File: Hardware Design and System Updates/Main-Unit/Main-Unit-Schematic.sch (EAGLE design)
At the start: 2 parts, among them U1 MSP430FR2110IPW16

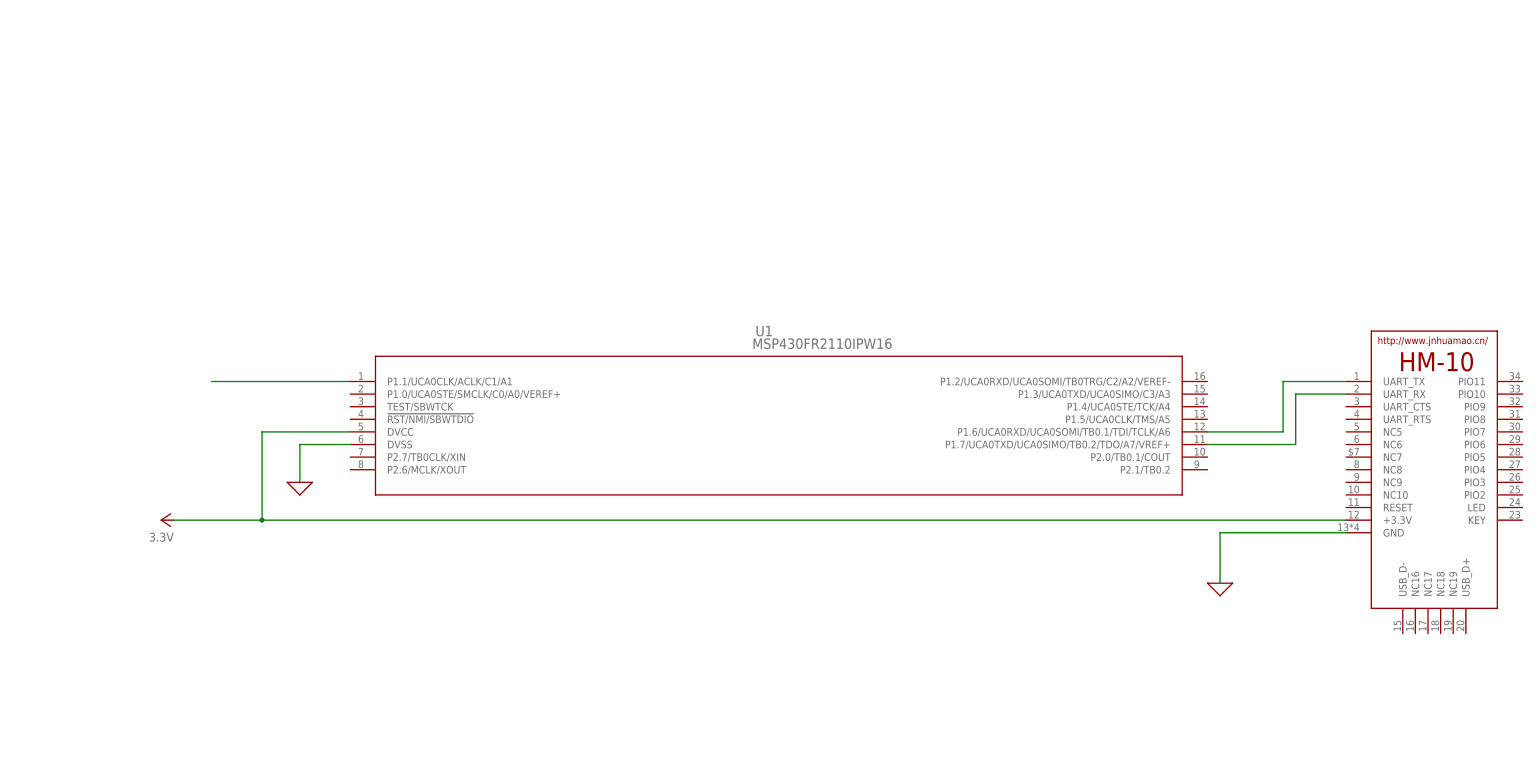
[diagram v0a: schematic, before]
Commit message: Fixed schematics
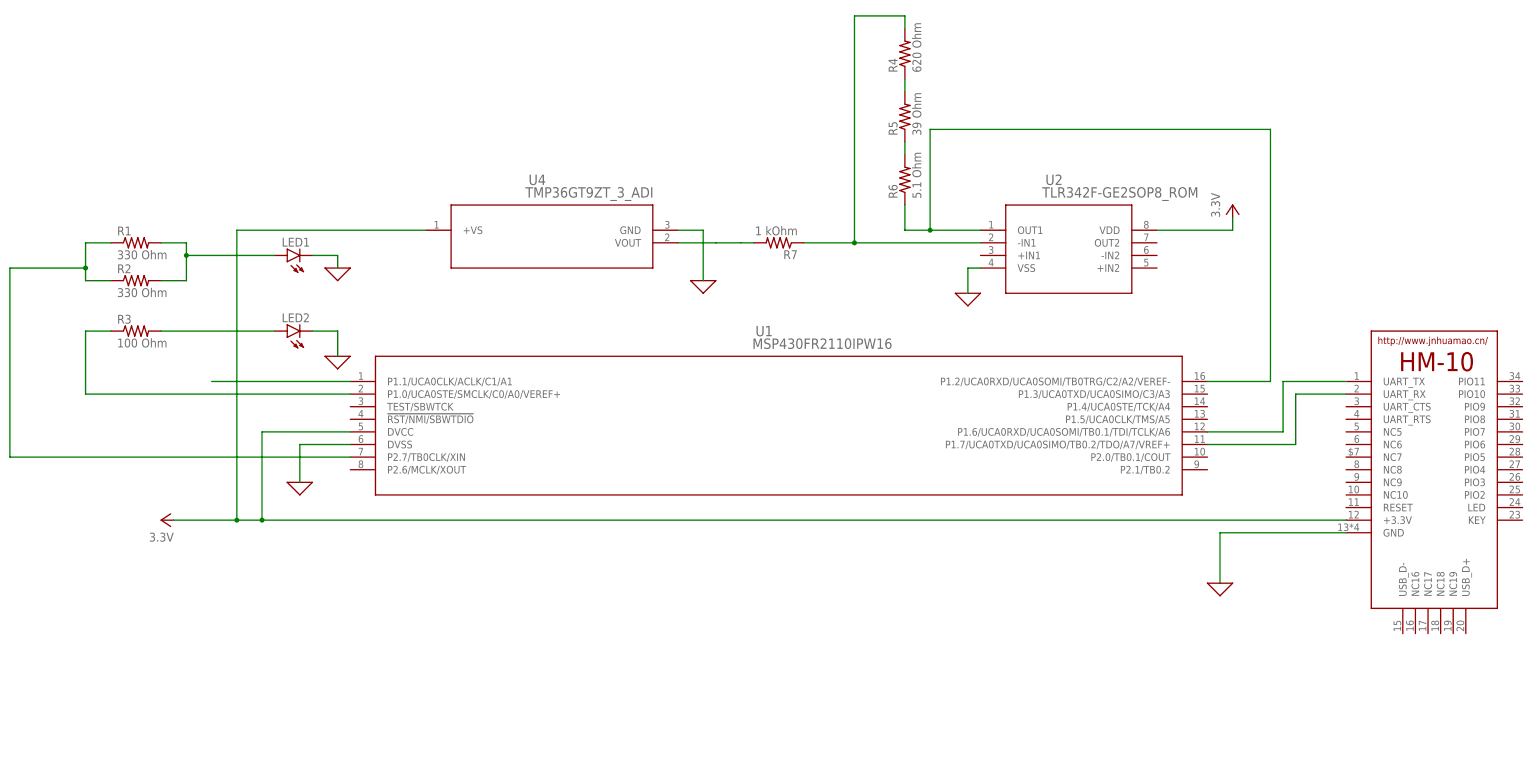
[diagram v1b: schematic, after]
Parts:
- added LED1, LED2: (no value), led:LED5MM
- added R1, R2: 330 Ohm, rcl:R-US_0204/7
- added R3: 100 Ohm, rcl:R-US_0204/7
- added R4: 620 Ohm, rcl:R-US_0204/7
- added R5: 39 Ohm, rcl:R-US_0204/7
- added R6: 5.1 Ohm, rcl:R-US_0204/7
- added R7: 1 kOhm, rcl:R-US_0204/7
- added U2: TLR342F-GE2SOP8_ROM, 2023-03-28_11-48-47_Library:TLR342F-GE2SOP8_ROM
- added U4: TMP36GT9ZT_3_ADI, 2023-03-28_14-12-25_Library:TMP36GT9ZT_3_ADI
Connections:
- new net N$10: R6.1, U1.P1.2/UCA0RXD/UCA0SOMI/TB0TRG/C2/A2/VEREF-, U2.OUT1
- new net N$11: R4.2, R7.1, U2.-IN1
- new net N$12: R7.2, U4.VOUT
- new net N$4: R1.1, R2.1, U1.P2.7/TB0CLK/XIN
- new net N$5: R3.1, U1.P1.0/UCA0STE/SMCLK/C0/A0/VEREF+
- new net N$6: LED1.A, R1.2, R2.2
- new net N$7: LED2.A, R3.2
- new net N$8: R4.1, R5.2
- new net N$9: R5.1, R6.2
- net 0: now also LED1.C, LED2.C, U2.VSS, U4.GND
- net VCC: now also U2.VDD, U4.+VS

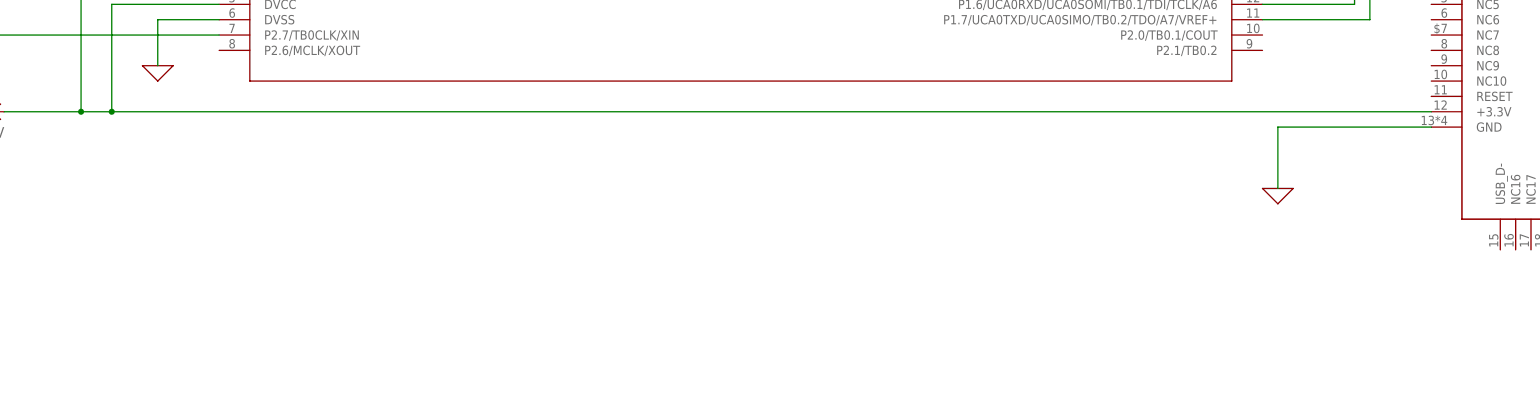
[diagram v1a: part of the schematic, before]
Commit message: Added 5v regulator to schematics
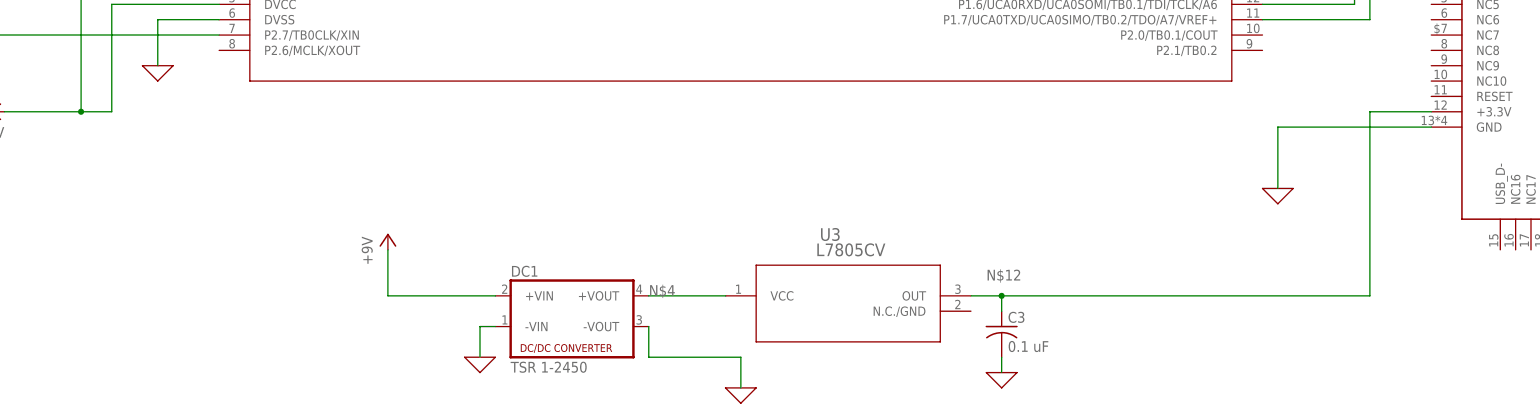
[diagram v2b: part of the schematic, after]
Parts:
- added C3: 0.1 uF, rcl:C-US050-024X044
- added DC1: TSR 1-2450, dc-dc-converter:NME
- added U3: L7805CV, 2023-03-08_12-17-23_Library:BA033CC0FP-E2TO252-3_ROM
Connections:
- new net +5V: DC1.+VIN
- net 0: now also C3.2, DC1.-VIN, DC1.-VOUT
- net N$12: now also C3.1, E1.+3.3V, U3.OUT
- net N$4: now also DC1.+VOUT, U3.VCC
- net VCC: no longer E1.+3.3V
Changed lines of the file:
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@@
 <part name="U4" library="2023-03-28_14-12-25_Library" deviceset="TMP36GT9Z" device="T_3_ADI"/>
 <part name="X_7" library="ngspice-simulation" library_urn="urn:adsk.eagle:library:527439" deviceset="GND" device=""/>
+<part name="DC1" library="dc-dc-converter" library_urn="urn:adsk.eagle:library:208" deviceset="NME" device="" package3d_urn="urn:adsk.eagle:package:12313/1" value="TSR 1-2450"/>
+<part name="X_6" library="ngspice-simulation" library_urn="urn:adsk.eagle:library:527439" deviceset="GND" device=""/>
+<part name="U3" library="2023-03-08_12-17-23_Library" deviceset="BA033CC0FP-E2" device="TO252-3_ROM" value="L7805CV"/>
+<part name="X_8" library="ngspice-simulation" library_urn="urn:adsk.eagle:library:527439" deviceset="GND" device=""/>
+<part name="C3" library="rcl" library_urn="urn:adsk.eagle:library:334" deviceset="C-US" device="050-024X044" package3d_urn="urn:adsk.eagle:package:23643/1" value="0.1 uF"/>
+<part name="X_10" library="ngspice-simulation" library_urn="urn:adsk.eagle:library:527439" deviceset="GND" device=""/>
+<part name="P+3" library="supply1" library_urn="urn:adsk.eagle:library:371" deviceset="+5V" device="" value="+9V"/>
 </parts>
 <sheets>
@@
 </instance>
 <instance part="X_7" gate="G$1" x="68.58" y="81.28" smashed="yes"/>
+<instance part="DC1" gate="G$1" x="55.88" y="0" smashed="yes">
+<attribute name="NAME" x="45.72" y="5.715" size="1.778" layer="95"/>
+<attribute name="VALUE" x="45.72" y="-10.16" size="1.778" layer="96"/>
+</instance>
+<instance part="X_6" gate="G$1" x="40.64" y="-7.62" smashed="yes"/>
+<instance part="U3" gate="A" x="78.74" y="2.54" smashed="yes">
+<attribute name="NAME" x="96.8746" y="11.6586" size="2.083" layer="95" ratio="6"/>
+<attribute name="VALUE" x="96.2352" y="9.1186" size="2.083" layer="96" ratio="6"/>
+</instance>
+<instance part="X_8" gate="G$1" x="83.82" y="-12.7" smashed="yes"/>
+<instance part="C3" gate="G$1" x="127" y="-2.54" smashed="yes">
+<attribute name="NAME" x="128.016" y="-1.905" size="1.778" layer="95"/>
+<attribute name="VALUE" x="128.016" y="-6.731" size="1.778" layer="96"/>
+</instance>
+<instance part="X_10" gate="G$1" x="127" y="-10.16" smashed="yes"/>
+<instance part="P+3" gate="1" x="25.4" y="12.7" smashed="yes">
+<attribute name="VALUE" x="22.86" y="7.62" size="1.778" layer="96" rot="R90"/>
+</instance>
 </instances>
 <busses>
@@
 <wire x1="-2.54" y1="50.8" x2="-20.32" y2="50.8" width="0.1524" layer="91"/>
 <wire x1="-20.32" y1="50.8" x2="-20.32" y2="33.02" width="0.1524" layer="91"/>
-<pinref part="E1" gate="G$1" pin="+3.3V"/>
-<wire x1="-20.32" y1="33.02" x2="198.12" y2="33.02" width="0.1524" layer="91"/>
 <wire x1="-20.32" y1="33.02" x2="-25.4" y2="33.02" width="0.1524" layer="91"/>
-<junction x="-20.32" y="33.02"/>
 <pinref part="P+1" gate="VCC" pin="VCC"/>
 <pinref part="U4" gate="A" pin="+VS"/>
@@
 <wire x1="68.58" y1="91.44" x2="68.58" y2="81.28" width="0.1524" layer="91"/>
 <pinref part="X_7" gate="G$1" pin="0"/>
+</segment>
+<segment>
+<pinref part="X_6" gate="G$1" pin="0"/>
+<pinref part="DC1" gate="G$1" pin="-VIN"/>
+<wire x1="40.64" y1="-7.62" x2="40.64" y2="-2.54" width="0.1524" layer="91"/>
+<wire x1="40.64" y1="-2.54" x2="43.18" y2="-2.54" width="0.1524" layer="91"/>
+</segment>
+<segment>
+<pinref part="DC1" gate="G$1" pin="-VOUT"/>
+<wire x1="68.58" y1="-2.54" x2="68.58" y2="-7.62" width="0.1524" layer="91"/>
+<wire x1="68.58" y1="-7.62" x2="83.82" y2="-7.62" width="0.1524" layer="91"/>
+<pinref part="X_8" gate="G$1" pin="0"/>
+<wire x1="83.82" y1="-12.7" x2="83.82" y2="-7.62" width="0.1524" layer="91"/>
+</segment>
+<segment>
+<pinref part="X_10" gate="G$1" pin="0"/>
+<pinref part="C3" gate="G$1" pin="2"/>
+<wire x1="127" y1="-10.16" x2="127" y2="-7.62" width="0.1524" layer="91"/>
 </segment>
 </net>
@@
 <wire x1="-71.12" y1="45.72" x2="-2.54" y2="45.72" width="0.1524" layer="91"/>
 </segment>
+<segment>
+<pinref part="DC1" gate="G$1" pin="+VOUT"/>
+<wire x1="68.58" y1="2.54" x2="81.28" y2="2.54" width="0.1524" layer="91"/>
+<label x="68.58" y="2.54" size="1.778" layer="95"/>
+<pinref part="U3" gate="A" pin="VCC"/>
+</segment>
 </net>
 <net name="N$5" class="0">
@@
 <wire x1="71.12" y1="88.9" x2="76.2" y2="88.9" width="0.1524" layer="91"/>
 <wire x1="78.74" y1="88.9" x2="76.2" y2="88.9" width="0.1524" layer="91"/>
+</segment>
+<segment>
+<wire x1="121.92" y1="2.54" x2="127" y2="2.54" width="0.1524" layer="91"/>
+<label x="124.46" y="5.08" size="1.778" layer="95"/>
+<pinref part="U3" gate="A" pin="OUT"/>
+<pinref part="C3" gate="G$1" pin="1"/>
+<wire x1="127" y1="0" x2="127" y2="2.54" width="0.1524" layer="91"/>
+<junction x="127" y="2.54"/>
+<wire x1="127" y1="2.54" x2="187.96" y2="2.54" width="0.1524" layer="91"/>
+<wire x1="187.96" y1="2.54" x2="187.96" y2="33.02" width="0.1524" layer="91"/>
+<pinref part="E1" gate="G$1" pin="+3.3V"/>
+<wire x1="187.96" y1="33.02" x2="198.12" y2="33.02" width="0.1524" layer="91"/>
 </segment>
 </net>
@@
 </segment>
 </net>
+<net name="+5V" class="0">
+<segment>
+<pinref part="DC1" gate="G$1" pin="+VIN"/>
+<wire x1="25.4" y1="2.54" x2="43.18" y2="2.54" width="0.1524" layer="91"/>
+<pinref part="P+3" gate="1" pin="+5V"/>
+<wire x1="25.4" y1="2.54" x2="25.4" y2="10.16" width="0.1524" layer="91"/>
+</segment>
+</net>
